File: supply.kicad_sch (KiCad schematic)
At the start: 87 parts, among them U1 AP7330-W5-7, U2 AP7330-W5-7, U3 AP7330-W5-7, U4 AP62301WU-7, U5 AP62301WU-7, U6 AP62301WU-7, U8 NCV51200MNTXG

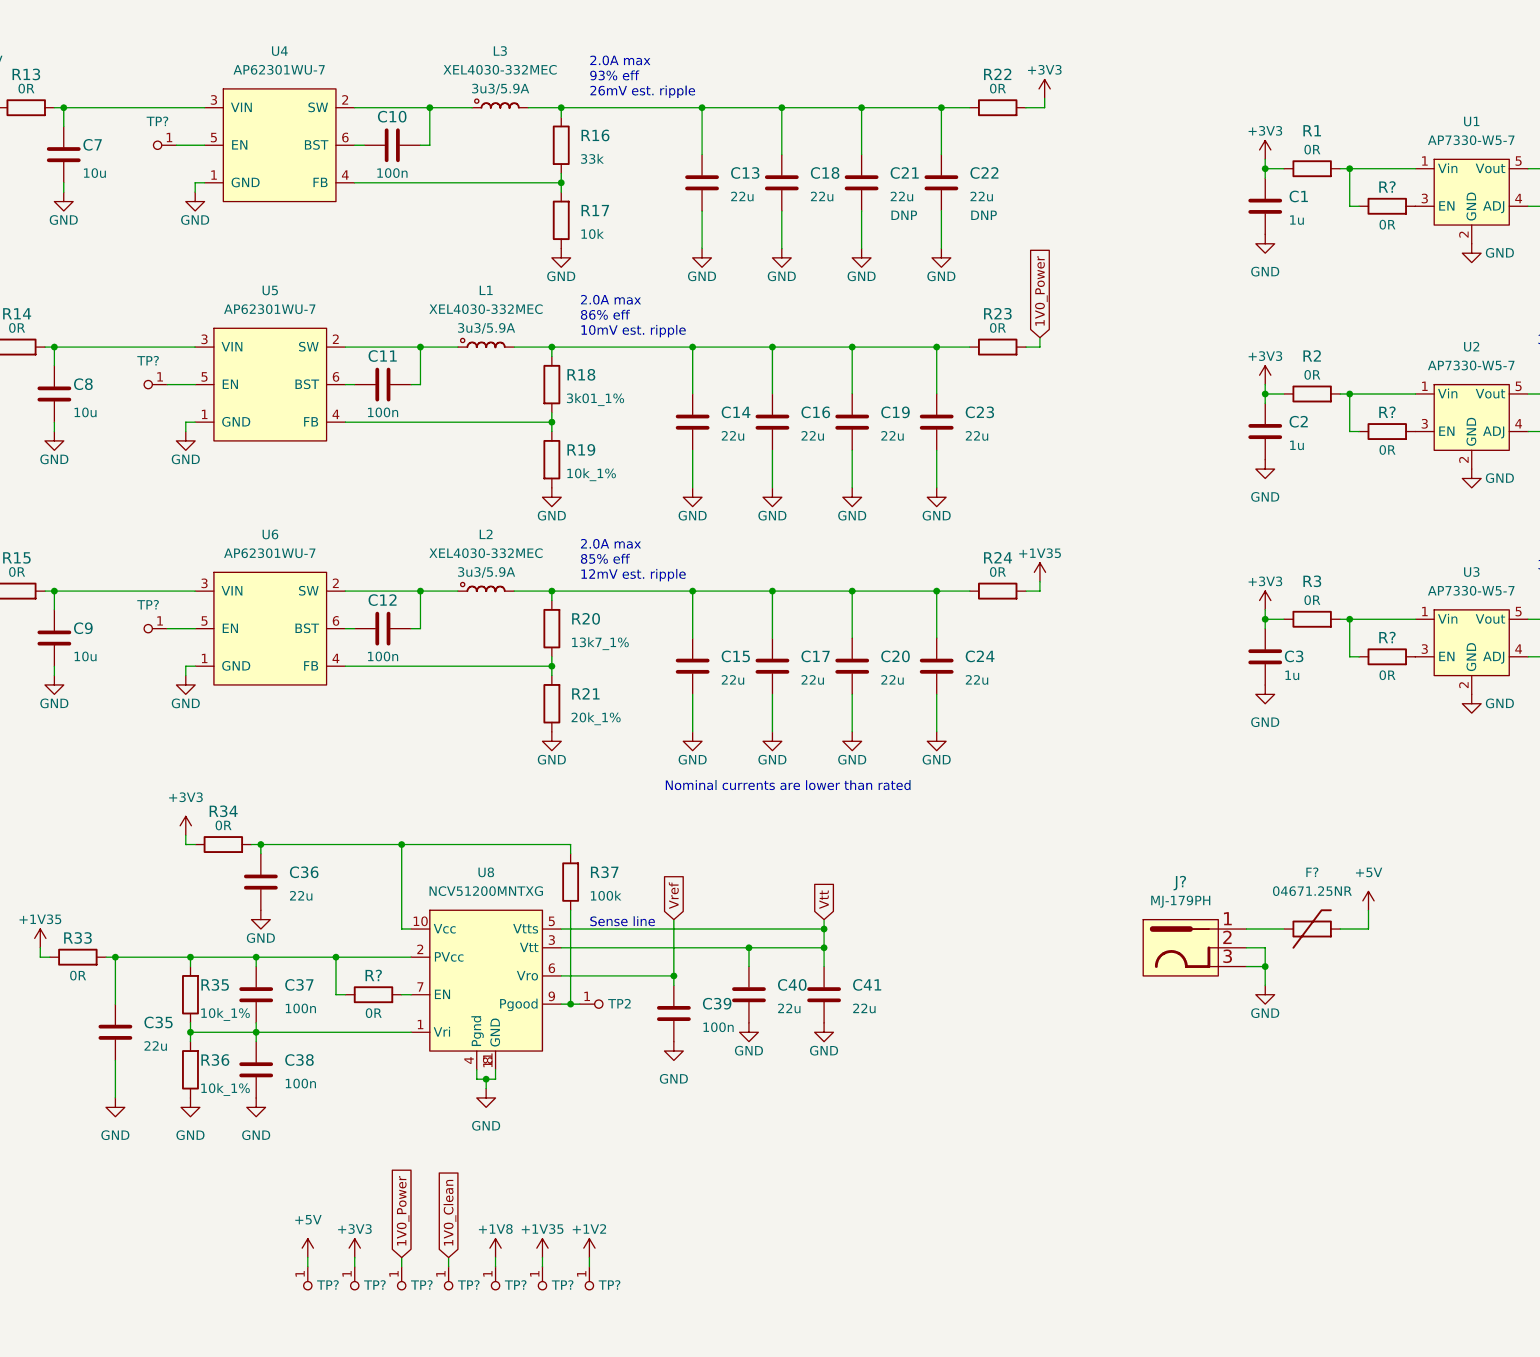
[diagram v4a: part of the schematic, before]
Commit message: Connected Semtech to the power supply, cable driver and the FPGA
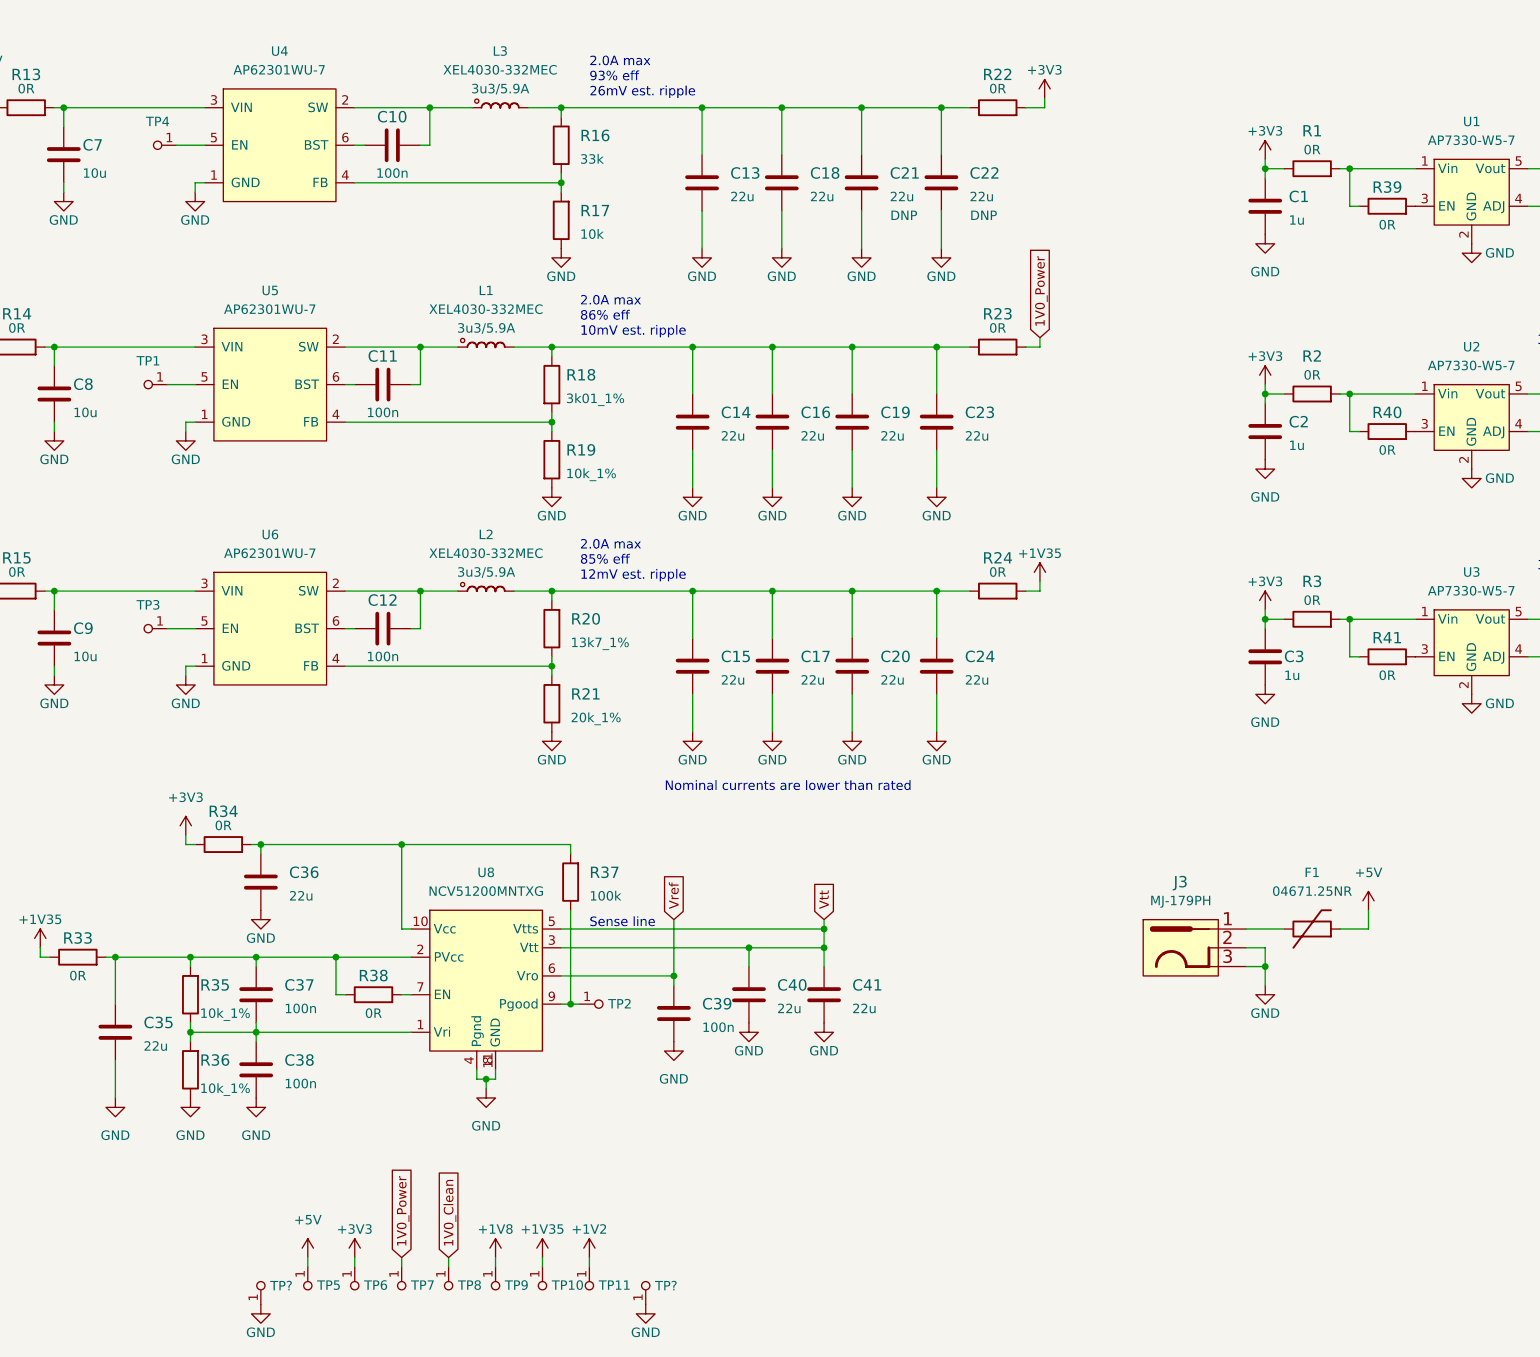
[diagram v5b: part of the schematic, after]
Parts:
- added TP? (x2): TP, antmicro-footprints:TP-R-1.5, symbol antmicroTestPoints:TP
- gave numbers to parts that had none: 16
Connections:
- net GND: now also TP?.1, TP?.1
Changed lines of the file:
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@@
   (symbol (lib_id "power:+5V") (at 67.31 180.34 0) (unit 1)
     (in_bom yes) (on_board yes) (fields_autoplaced)
-    (property "Reference" "#PWR?" (id 0) (at 67.31 184.15 0)
+    (property "Reference" "#PWR0211" (id 0) (at 67.31 184.15 0)
       (effects (font (size 1.27 1.27)) hide)
     )
@@
   (symbol (lib_id "power:+1V35") (at 99.06 180.34 0) (unit 1)
     (in_bom yes) (on_board yes)
-    (property "Reference" "#PWR?" (id 0) (at 99.06 184.15 0)
+    (property "Reference" "#PWR0213" (id 0) (at 99.06 184.15 0)
       (effects (font (size 1.27 1.27)) hide)
     )
@@
   (symbol (lib_id "antmicroTestPoints:TP") (at 92.71 184.15 0) (unit 1)
     (in_bom yes) (on_board yes) (fields_autoplaced)
-    (property "Reference" "TP?" (id 0) (at 93.98 184.1118 0)
+    (property "Reference" "TP9" (id 0) (at 93.98 184.1118 0)
       (effects (font (size 1.27 1.27)) (justify left))
     )
@@
   (symbol (lib_id "power:+1V2") (at 105.41 180.34 0) (unit 1)
     (in_bom yes) (on_board yes)
-    (property "Reference" "#PWR?" (id 0) (at 105.41 184.15 0)
+    (property "Reference" "#PWR0214" (id 0) (at 105.41 184.15 0)
       (effects (font (size 1.27 1.27)) hide)
     )
@@
     (pin "2")
   )
+  (symbol (lib_id "power:GND") (at 113.03 186.69 0) (unit 1)
+    (in_bom yes) (on_board yes)
+    (property "Reference" "#PWR?" (id 0) (at 113.03 193.04 0)
+      (effects (font (size 1.27 1.27)) hide)
+    )
+    (property "Value" "GND" (id 1) (at 113.03 190.5 0))
+    (property "Footprint" "" (id 2) (at 113.03 186.69 0)
+      (effects (font (size 1.27 1.27)) hide)
+    )
+    (property "Datasheet" "" (id 3) (at 113.03 186.69 0)
+      (effects (font (size 1.27 1.27)) hide)
+    )
+    (pin "1")
+  )
+  (symbol (lib_id "power:GND") (at 60.96 186.69 0) (unit 1)
+    (in_bom yes) (on_board yes)
+    (property "Reference" "#PWR?" (id 0) (at 60.96 193.04 0)
+      (effects (font (size 1.27 1.27)) hide)
+    )
+    (property "Value" "GND" (id 1) (at 60.96 190.5 0))
+    (property "Footprint" "" (id 2) (at 60.96 186.69 0)
+      (effects (font (size 1.27 1.27)) hide)
+    )
+    (property "Datasheet" "" (id 3) (at 60.96 186.69 0)
+      (effects (font (size 1.27 1.27)) hide)
+    )
+    (pin "1")
+  )
   (symbol (lib_id "power:GND") (at 100.33 76.2 0) (unit 1)
     (in_bom yes) (on_board yes)
@@
   (symbol (lib_id "antmicroResistors0603:R_0R_0603") (at 213.36 99.06 0) (unit 1)
     (in_bom yes) (on_board yes)
-    (property "Reference" "R?" (id 0) (at 213.36 96.52 0)
+    (property "Reference" "R41" (id 0) (at 213.36 96.52 0)
       (effects (font (size 1.524 1.524)))
     )
@@
     (pin "2")
   )
+  (symbol (lib_id "antmicroTestPoints:TP") (at 113.03 184.15 180) (unit 1)
+    (in_bom yes) (on_board yes) (fields_autoplaced)
+    (property "Reference" "TP?" (id 0) (at 114.3 184.188 0)
+      (effects (font (size 1.27 1.27)) (justify right))
+    )
+    (property "Value" "TP" (id 1) (at 113.03 184.15 0)
+      (effects (font (size 1.27 1.27)) hide)
+    )
+    (property "Footprint" "antmicro-footprints:TP-R-1.5" (id 2) (at 113.03 184.15 0)
+      (effects (font (size 1.27 1.27)) hide)
+    )
+    (property "Datasheet" "" (id 3) (at 113.03 184.15 0)
+      (effects (font (size 1.27 1.27)) hide)
+    )
+    (pin "1")
+  )
   (symbol (lib_id "power:GND") (at 41.275 158.75 0) (unit 1)
     (in_bom yes) (on_board yes) (fields_autoplaced)
@@
     (pin "1")
   )
+  (symbol (lib_id "antmicroTestPoints:TP") (at 60.96 184.15 180) (unit 1)
+    (in_bom yes) (on_board yes) (fields_autoplaced)
+    (property "Reference" "TP?" (id 0) (at 62.23 184.188 0)
+      (effects (font (size 1.27 1.27)) (justify right))
+    )
+    (property "Value" "TP" (id 1) (at 60.96 184.15 0)
+      (effects (font (size 1.27 1.27)) hide)
+    )
+    (property "Footprint" "antmicro-footprints:TP-R-1.5" (id 2) (at 60.96 184.15 0)
+      (effects (font (size 1.27 1.27)) hide)
+    )
+    (property "Datasheet" "" (id 3) (at 60.96 184.15 0)
+      (effects (font (size 1.27 1.27)) hide)
+    )
+    (pin "1")
+  )
   (symbol (lib_id "antmicroCapacitors0603:C_10u_0603") (at 33.02 96.52 0) (unit 1)
     (in_bom yes) (on_board yes)
@@
   (symbol (lib_id "antmicroTestPoints:TP") (at 45.72 95.25 270) (unit 1)
     (in_bom yes) (on_board yes) (fields_autoplaced)
-    (property "Reference" "TP?" (id 0) (at 45.7581 92.075 90))
+    (property "Reference" "TP3" (id 0) (at 45.7581 92.075 90))
     (property "Value" "TP" (id 1) (at 45.72 95.25 0)
       (effects (font (size 1.27 1.27)) hide)
@@
   (symbol (lib_id "antmicroResistors0603:R_0R_0603") (at 213.36 68.58 0) (unit 1)
     (in_bom yes) (on_board yes)
-    (property "Reference" "R?" (id 0) (at 213.36 66.04 0)
+    (property "Reference" "R40" (id 0) (at 213.36 66.04 0)
       (effects (font (size 1.524 1.524)))
     )
@@
   (symbol (lib_id "antmicroTestPoints:TP") (at 73.66 184.15 0) (unit 1)
     (in_bom yes) (on_board yes) (fields_autoplaced)
-    (property "Reference" "TP?" (id 0) (at 74.93 184.1118 0)
+    (property "Reference" "TP6" (id 0) (at 74.93 184.1118 0)
       (effects (font (size 1.27 1.27)) (justify left))
     )
@@
   (symbol (lib_id "antmicroTestPoints:TP") (at 80.01 184.15 0) (unit 1)
     (in_bom yes) (on_board yes) (fields_autoplaced)
-    (property "Reference" "TP?" (id 0) (at 81.28 184.1118 0)
+    (property "Reference" "TP7" (id 0) (at 81.28 184.1118 0)
       (effects (font (size 1.27 1.27)) (justify left))
     )
@@
   (symbol (lib_id "antmicroTestPoints:TP") (at 67.31 184.15 0) (unit 1)
     (in_bom yes) (on_board yes) (fields_autoplaced)
-    (property "Reference" "TP?" (id 0) (at 68.58 184.1118 0)
+    (property "Reference" "TP5" (id 0) (at 68.58 184.1118 0)
       (effects (font (size 1.27 1.27)) (justify left))
     )
@@
   (symbol (lib_id "power:+5V") (at 210.82 133.35 0) (unit 1)
     (in_bom yes) (on_board yes) (fields_autoplaced)
-    (property "Reference" "#PWR?" (id 0) (at 210.82 137.16 0)
+    (property "Reference" "#PWR0215" (id 0) (at 210.82 137.16 0)
       (effects (font (size 1.27 1.27)) hide)
     )
@@
   (symbol (lib_id "power:+1V8") (at 92.71 180.34 0) (unit 1)
     (in_bom yes) (on_board yes)
-    (property "Reference" "#PWR?" (id 0) (at 92.71 184.15 0)
+    (property "Reference" "#PWR0212" (id 0) (at 92.71 184.15 0)
       (effects (font (size 1.27 1.27)) hide)
     )
@@
   (symbol (lib_id "power:+3V3") (at 73.66 180.34 0) (unit 1)
     (in_bom yes) (on_board yes)
-    (property "Reference" "#PWR?" (id 0) (at 73.66 184.15 0)
+    (property "Reference" "#PWR0210" (id 0) (at 73.66 184.15 0)
       (effects (font (size 1.27 1.27)) hide)
     )
@@
   (symbol (lib_id "antmicroResistors0603:R_0R_0603") (at 76.2 144.78 0) (unit 1)
     (in_bom yes) (on_board yes)
-    (property "Reference" "R?" (id 0) (at 76.2 142.24 0)
+    (property "Reference" "R38" (id 0) (at 76.2 142.24 0)
       (effects (font (size 1.524 1.524)))
     )
@@
   (symbol (lib_id "power:GND") (at 196.85 143.51 0) (unit 1)
     (in_bom yes) (on_board yes)
-    (property "Reference" "#PWR?" (id 0) (at 196.85 149.86 0)
+    (property "Reference" "#PWR0216" (id 0) (at 196.85 149.86 0)
       (effects (font (size 1.27 1.27)) hide)
     )
@@
   (symbol (lib_id "antmicroTestPoints:TP") (at 86.36 184.15 0) (unit 1)
     (in_bom yes) (on_board yes) (fields_autoplaced)
-    (property "Reference" "TP?" (id 0) (at 87.63 184.1118 0)
+    (property "Reference" "TP8" (id 0) (at 87.63 184.1118 0)
       (effects (font (size 1.27 1.27)) (justify left))
     )
@@
   (symbol (lib_id "antmicroBarrelAudioConnectors:DC_SOCKET") (at 189.23 138.43 0) (unit 1)
     (in_bom yes) (on_board yes) (fields_autoplaced)
-    (property "Reference" "J?" (id 0) (at 185.42 129.54 0)
+    (property "Reference" "J3" (id 0) (at 185.42 129.54 0)
       (effects (font (size 1.524 1.524)))
     )
@@
   (symbol (lib_id "antmicroTestPoints:TP") (at 45.72 62.23 270) (unit 1)
     (in_bom yes) (on_board yes) (fields_autoplaced)
-    (property "Reference" "TP?" (id 0) (at 45.7581 59.055 90))
+    (property "Reference" "TP1" (id 0) (at 45.7581 59.055 90))
     (property "Value" "TP" (id 1) (at 45.72 62.23 0)
       (effects (font (size 1.27 1.27)) hide)
@@
   (symbol (lib_id "antmicroResistors0603:R_0R_0603") (at 213.36 38.1 0) (unit 1)
     (in_bom yes) (on_board yes)
-    (property "Reference" "R?" (id 0) (at 213.36 35.56 0)
+    (property "Reference" "R39" (id 0) (at 213.36 35.56 0)
       (effects (font (size 1.524 1.524)))
     )
@@
   (symbol (lib_id "antmicroTestPoints:TP") (at 46.99 29.845 270) (unit 1)
     (in_bom yes) (on_board yes) (fields_autoplaced)
-    (property "Reference" "TP?" (id 0) (at 47.0281 26.67 90))
+    (property "Reference" "TP4" (id 0) (at 47.0281 26.67 90))
     (property "Value" "TP" (id 1) (at 46.99 29.845 0)
       (effects (font (size 1.27 1.27)) hide)
@@
   (symbol (lib_id "antmicroTestPoints:TP") (at 99.06 184.15 0) (unit 1)
     (in_bom yes) (on_board yes) (fields_autoplaced)
-    (property "Reference" "TP?" (id 0) (at 100.33 184.1118 0)
+    (property "Reference" "TP10" (id 0) (at 100.33 184.1118 0)
       (effects (font (size 1.27 1.27)) (justify left))
     )
@@
   (symbol (lib_id "antmicroFuses:04671.25NR") (at 203.2 135.89 0) (unit 1)
     (in_bom yes) (on_board yes) (fields_autoplaced)
-    (property "Reference" "F?" (id 0) (at 203.2 128.27 0))
+    (property "Reference" "F1" (id 0) (at 203.2 128.27 0))
     (property "Value" "04671.25NR" (id 1) (at 203.2 130.81 0))
     (property "Footprint" "antmicro-footprints:0603-Fuse-Littelfuse-0467" (id 2) (at 204.47 141.605 0)
@@
   (symbol (lib_id "antmicroTestPoints:TP") (at 105.41 184.15 0) (unit 1)
     (in_bom yes) (on_board yes) (fields_autoplaced)
-    (property "Reference" "TP?" (id 0) (at 106.68 184.1118 0)
-      (effects (font (size 1.27 1.27)) (justify left))
-    )
+    (property "Reference" "TP11" (id 0) (at 106.68 184.1118 0)
+      (effects (font (size 1.27 1.27)) (justify left))
+    )
